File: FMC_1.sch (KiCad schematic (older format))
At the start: 16 parts, among them P1 SAMTEC_ASP-134603-01

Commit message: Convert all footprints to use Marble nickname
Includes both .sch and .lib files
Includes both bare footprint names and those with CERN-like nicknames
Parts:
- C61: footprint CAPC1005X55N -> Marble:CAPC1005X55N
- C62: footprint CAPC3216X140N -> Marble:CAPC3216X140N
- C63, C64, C65, C66, C67: footprint CAPC0603X33N -> Marble:CAPC0603X33N
- C68, C69: footprint CAPC1608X87N -> Marble:CAPC1608X87N
- F2: footprint FUSC1608X55N -> Marble:FUSC1608X55N
- P1: footprint SAMTEC_ASP-134603-01 -> Marble:SAMTEC_ASP-134603-01
- R234, R260, R261: footprint RESC1005X40N -> Marble:RESC1005X40N
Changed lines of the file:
@@
 F 0 "R234" V 10454 1260 50  0000 L CNN
 F 1 "R0402_10K_1%_0.0625W_100PPM" H 10350 990 60  0001 L CNN
-F 2 "RESC1005X40N" H 10350 180 60  0001 L CNN
+F 2 "Marble:RESC1005X40N" H 10350 180 60  0001 L CNN
 F 3 "\\\\cern.ch\\dfs\\Applications\\Altium\\Datasheets\\R0402_Phycomp_RC0402.pdf" H 10350 810 60  0001 L CNN
 F 4 "10k" V 10545 1260 50  0000 L CNN "~"
@@
 F 0 "C68" V 7796 5690 50  0000 R CNN
 F 1 "CC0603_10UF_6.3V_20%_X5R" H 7600 5540 60  0001 L CNN
-F 2 "CAPC1608X87N" H 7600 4730 60  0001 L CNN
+F 2 "Marble:CAPC1608X87N" H 7600 4730 60  0001 L CNN
 F 3 "\\\\cern.ch\\dfs\\Applications\\Altium\\Datasheets\\CC0603_X5R_KEMET.pdf" H 7600 5360 60  0001 L CNN
 F 4 "10uF" V 7705 5690 50  0000 R CNN "~"
@@
 F 0 "C67" V 7204 5610 50  0000 L CNN
 F 1 "CC0201_100NF_6.3V_10%_X5R" H 7100 5240 60  0001 L CNN
-F 2 "CAPC0603X33N" H 7100 4430 60  0001 L CNN
+F 2 "Marble:CAPC0603X33N" H 7100 4430 60  0001 L CNN
 F 3 "\\\\cern.ch\\dfs\\Applications\\Altium\\Datasheets\\CC0201_X5R_AVX.pdf" H 7100 5060 60  0001 L CNN
 F 4 "100nF" V 7295 5610 50  0000 L CNN "~"
@@
 F 0 "C69" V 8196 5690 50  0000 R CNN
 F 1 "CC0603_10UF_6.3V_20%_X5R" H 8000 5540 60  0001 L CNN
-F 2 "CAPC1608X87N" H 8000 4730 60  0001 L CNN
+F 2 "Marble:CAPC1608X87N" H 8000 4730 60  0001 L CNN
 F 3 "\\\\cern.ch\\dfs\\Applications\\Altium\\Datasheets\\CC0603_X5R_KEMET.pdf" H 8000 5360 60  0001 L CNN
 F 4 "10uF" V 8105 5690 50  0000 R CNN "~"
@@
 F 0 "C65" V 5754 6710 50  0000 L CNN
 F 1 "CC0201_100NF_6.3V_10%_X5R" H 5650 6340 60  0001 L CNN
-F 2 "CAPC0603X33N" H 5650 5530 60  0001 L CNN
+F 2 "Marble:CAPC0603X33N" H 5650 5530 60  0001 L CNN
 F 3 "\\\\cern.ch\\dfs\\Applications\\Altium\\Datasheets\\CC0201_X5R_AVX.pdf" H 5650 6160 60  0001 L CNN
 F 4 "100nF" V 5845 6710 50  0000 L CNN "~"
@@
 F 0 "C66" V 6204 6710 50  0000 L CNN
 F 1 "CC0201_100NF_6.3V_10%_X5R" H 6100 6340 60  0001 L CNN
-F 2 "CAPC0603X33N" H 6100 5530 60  0001 L CNN
+F 2 "Marble:CAPC0603X33N" H 6100 5530 60  0001 L CNN
 F 3 "\\\\cern.ch\\dfs\\Applications\\Altium\\Datasheets\\CC0201_X5R_AVX.pdf" H 6100 6160 60  0001 L CNN
 F 4 "100nF" V 6295 6710 50  0000 L CNN "~"
@@
 F 0 "C63" V 4504 5810 50  0000 L CNN
 F 1 "CC0201_100NF_6.3V_10%_X5R" H 4400 5440 60  0001 L CNN
-F 2 "CAPC0603X33N" H 4400 4630 60  0001 L CNN
+F 2 "Marble:CAPC0603X33N" H 4400 4630 60  0001 L CNN
 F 3 "\\\\cern.ch\\dfs\\Applications\\Altium\\Datasheets\\CC0201_X5R_AVX.pdf" H 4400 5260 60  0001 L CNN
 F 4 "100nF" V 4595 5810 50  0000 L CNN "~"
@@
 F 0 "C64" V 4954 5810 50  0000 L CNN
 F 1 "CC0201_100NF_6.3V_10%_X5R" H 4850 5440 60  0001 L CNN
-F 2 "CAPC0603X33N" H 4850 4630 60  0001 L CNN
+F 2 "Marble:CAPC0603X33N" H 4850 4630 60  0001 L CNN
 F 3 "\\\\cern.ch\\dfs\\Applications\\Altium\\Datasheets\\CC0201_X5R_AVX.pdf" H 4850 5260 60  0001 L CNN
 F 4 "100nF" V 5045 5810 50  0000 L CNN "~"
@@
 F 0 "C62" V 2804 5160 50  0000 L CNN
 F 1 "CC1206_10UF_16V_10%_X7R" H 2700 4790 60  0001 L CNN
-F 2 "CAPC3216X140N" H 2700 3980 60  0001 L CNN
+F 2 "Marble:CAPC3216X140N" H 2700 3980 60  0001 L CNN
 F 3 "\\\\cern.ch\\dfs\\Applications\\Altium\\Datasheets\\CC1206_X7R_KEMET.pdf" H 2700 4610 60  0001 L CNN
 F 4 "10uF" V 2895 5160 50  0000 L CNN "~"
@@
 F 0 "C61" V 2250 5050 50  0000 L CNN
 F 1 "CC0402_100NF_16V_10%_X5R" H 2200 4790 60  0001 L CNN
-F 2 "CAPC1005X55N" H 2200 3980 60  0001 L CNN
+F 2 "Marble:CAPC1005X55N" H 2200 3980 60  0001 L CNN
 F 3 "\\\\cern.ch\\dfs\\Applications\\Altium\\Datasheets\\CC0402_X5R_MURATA_GRM.pdf" H 2200 4610 60  0001 L CNN
 F 4 "100nF" V 2450 5050 50  0000 L CNN "~"
@@
 F 0 "F2" H 6700 6797 50  0000 C CNN
 F 1 "FUS0603_BOURNS-SF-0603F050-2" H 6550 6380 60  0001 L CNN
-F 2 "FUSC1608X55N" H 6550 5570 60  0001 L CNN
+F 2 "Marble:FUSC1608X55N" H 6550 5570 60  0001 L CNN
 F 3 "\\\\cern.ch\\dfs\\Applications\\Altium\\Datasheets\\FUSE_BOURNS_SF-0603F.pdf" H 6550 6200 60  0001 L CNN
 F 4 "500mA-50V" H 6700 6706 50  0000 C CNN "~"
@@
 F 0 "P1" H 4077 -500 50  0000 L CNN
 F 1 "SAMTEC_ASP-134603-01" H 3750 -2640 60  0001 L CNN
-F 2 "SAMTEC_ASP-134603-01" H 3750 -3540 60  0001 L CNN
+F 2 "Marble:SAMTEC_ASP-134603-01" H 3750 -3540 60  0001 L CNN
 F 3 "\\\\cern.ch\\dfs\\Applications\\Altium\\Datasheets\\SAMTEC_ASP-134603-01.pdf" H 3750 -2820 60  0001 L CNN
 F 4 "VITA 57" H 3750 -2910 60  0001 L CNN "Pole4"
@@
 F 0 "P1" H 6378 -500 50  0000 L CNN
 F 1 "SAMTEC_ASP-134603-01" H 6050 -2640 60  0001 L CNN
-F 2 "SAMTEC_ASP-134603-01" H 6050 -3540 60  0001 L CNN
+F 2 "Marble:SAMTEC_ASP-134603-01" H 6050 -3540 60  0001 L CNN
 F 3 "\\\\cern.ch\\dfs\\Applications\\Altium\\Datasheets\\SAMTEC_ASP-134603-01.pdf" H 6050 -2820 60  0001 L CNN
 F 4 "VITA 57" H 6050 -2910 60  0001 L CNN "Pole4"
@@
 F 0 "P1" H 9128 -500 50  0000 L CNN
 F 1 "SAMTEC_ASP-134603-01" H 8800 -2640 60  0001 L CNN
-F 2 "SAMTEC_ASP-134603-01" H 8800 -3540 60  0001 L CNN
+F 2 "Marble:SAMTEC_ASP-134603-01" H 8800 -3540 60  0001 L CNN
 F 3 "\\\\cern.ch\\dfs\\Applications\\Altium\\Datasheets\\SAMTEC_ASP-134603-01.pdf" H 8800 -2820 60  0001 L CNN
 F 4 "VITA 57" H 8800 -2910 60  0001 L CNN "Pole4"
@@
 F 0 "P1" H 11778 -500 50  0000 L CNN
 F 1 "SAMTEC_ASP-134603-01" H 11450 -2640 60  0001 L CNN
-F 2 "SAMTEC_ASP-134603-01" H 11450 -3540 60  0001 L CNN
+F 2 "Marble:SAMTEC_ASP-134603-01" H 11450 -3540 60  0001 L CNN
 F 3 "\\\\cern.ch\\dfs\\Applications\\Altium\\Datasheets\\SAMTEC_ASP-134603-01.pdf" H 11450 -2820 60  0001 L CNN
 F 4 "VITA 57" H 11450 -2910 60  0001 L CNN "Pole4"
@@
 F 0 "R260" V 5154 6660 50  0000 L CNN
 F 1 "R0402_10K_1%_0.0625W_100PPM" H 5050 6390 60  0001 L CNN
-F 2 "RESC1005X40N" H 5050 5580 60  0001 L CNN
+F 2 "Marble:RESC1005X40N" H 5050 5580 60  0001 L CNN
 F 3 "\\\\cern.ch\\dfs\\Applications\\Altium\\Datasheets\\R0402_Phycomp_RC0402.pdf" H 5050 6210 60  0001 L CNN
 F 4 "10k" V 5245 6660 50  0000 L CNN "~"
@@
 F 0 "R261" H 5550 6500 50  0000 L CNN
 F 1 "R0402_1K_1%_0.0625W_100PPM" H 5500 6390 60  0001 L CNN
-F 2 "RESC1005X40N" H 5500 5580 60  0001 L CNN
+F 2 "Marble:RESC1005X40N" H 5500 5580 60  0001 L CNN
 F 3 "\\\\cern.ch\\dfs\\Applications\\Altium\\Datasheets\\R0402_Phycomp_RC0402.pdf" H 5500 6210 60  0001 L CNN
 F 4 "1k" H 5600 6700 50  0000 L CNN "~"

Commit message: Get rid of most .DbLib suffixes in Library Name attributes
Enough that KiBoM no longer complains about them
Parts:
- R297, R298: Library Name Resistors.DbLib -> Resistors SMD
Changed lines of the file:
@@
 F 37 "10/17/12 00:00:00" H 2800 2130 50  0001 L CNN "LatestRevisionDate"
 F 38 "Resistors SMD" H 2800 2055 50  0001 L CNN "Database Table Name"
-F 39 "Resistors.DbLib" H 2800 1980 50  0001 L CNN "Library Name"
+F 39 "Resistors SMD" H 2800 1980 50  0001 L CNN "Library Name"
 F 40 "Resistors SMD" H 2800 1905 50  0001 L CNN "Footprint Library"
 F 41 "This work is licensed under the Creative Commons CC-BY-SA 4.0 License. To the extent that circuit schematics that use Licensed Material can be considered to be ‘Adapted Material’, then the copyright holder waives article 3.b of the license with respect to these schematics." H 2800 1830 50  0001 L CNN "License"
@@
 F 37 "10/17/12 00:00:00" H 4850 2230 50  0001 L CNN "LatestRevisionDate"
 F 38 "Resistors SMD" H 4850 2155 50  0001 L CNN "Database Table Name"
-F 39 "Resistors.DbLib" H 4850 2080 50  0001 L CNN "Library Name"
+F 39 "Resistors SMD" H 4850 2080 50  0001 L CNN "Library Name"
 F 40 "Resistors SMD" H 4850 2005 50  0001 L CNN "Footprint Library"
 F 41 "This work is licensed under the Creative Commons CC-BY-SA 4.0 License. To the extent that circuit schematics that use Licensed Material can be considered to be ‘Adapted Material’, then the copyright holder waives article 3.b of the license with respect to these schematics." H 4850 1930 50  0001 L CNN "License"

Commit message: Get rid of more useless inconsistencies in Comment attributes
Makes for quieter KiBoM runs
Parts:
- R297, R298: Comment 240 -> =Value
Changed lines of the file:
@@
 F 6 "Resistor - 1%" H 2800 4455 50  0001 L CNN "Library Ref"
 F 7 "SchLib\\Resistors.SchLib" H 2800 4380 50  0001 L CNN "Library Path"
-F 8 "240" H 2800 4305 50  0001 L CNN "Comment"
+F 8 "=Value" H 2800 4305 50  0001 L CNN "Comment"
 F 9 "Standard" H 2800 4230 50  0001 L CNN "Component Kind"
 F 10 "Standard" H 2800 4155 50  0001 L CNN "Component Type"
@@
 F 6 "Resistor - 1%" H 4850 4555 50  0001 L CNN "Library Ref"
 F 7 "SchLib\\Resistors.SchLib" H 4850 4480 50  0001 L CNN "Library Path"
-F 8 "240" H 4850 4405 50  0001 L CNN "Comment"
+F 8 "=Value" H 4850 4405 50  0001 L CNN "Comment"
 F 9 "Standard" H 4850 4330 50  0001 L CNN "Component Kind"
 F 10 "Standard" H 4850 4255 50  0001 L CNN "Component Type"

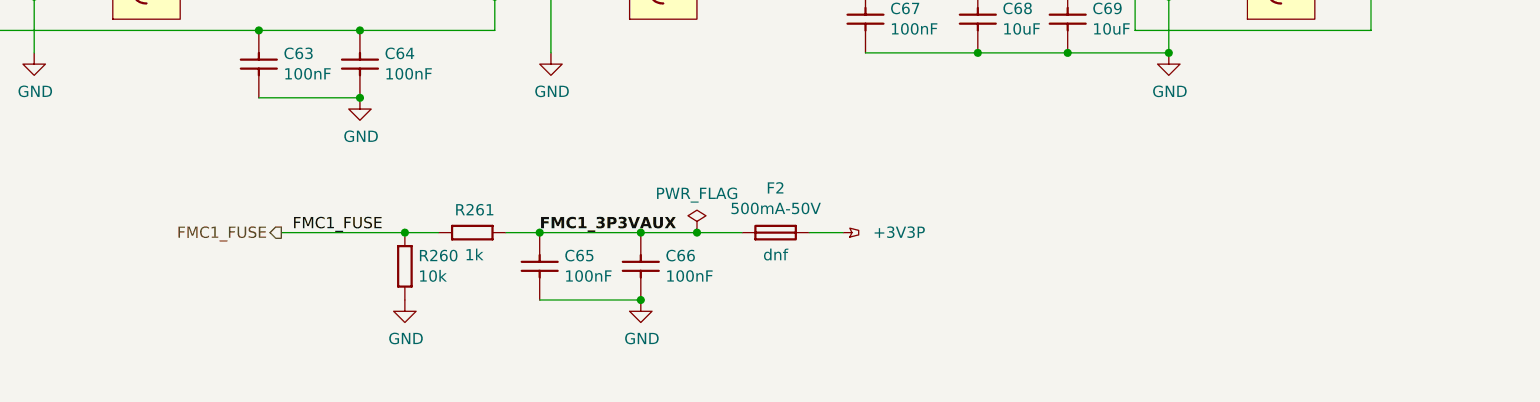
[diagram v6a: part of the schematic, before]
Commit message: added MIC2090-1
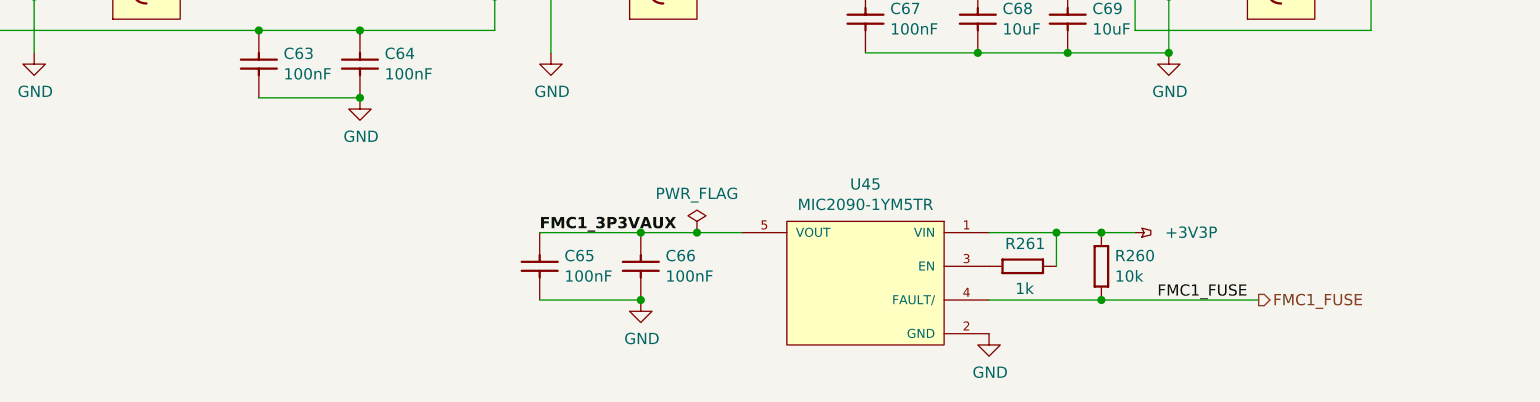
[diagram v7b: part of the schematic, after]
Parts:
- removed F2: FUS0603_BOURNS-SF-0603F050-2, Marble:FUSC1608X55N, symbol Fuses:FUS0603_BOURNS-SF-0603F050-2
- added U45: MIC2090-1YM5TR, ICs And Semiconductors SMD:SOT95P280X145-5N, symbol Analog_&_Interface:MIC2090-1YM5TR
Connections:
- net +3V3P: now also R260.1, R261.1, U45.1 (VIN)
- net FMC1_3P3VAUX: now also U45.5 (VOUT); no longer R261.1
- net FMC1_FUSE: now also R260.2, U45.4 (FAULT/); no longer R260.1, R261.2
- net GND: now also U45.2 (GND); no longer R260.2
- new net: R261.2, U45.3 (EN)
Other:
- moved on the sheet: R260, R261

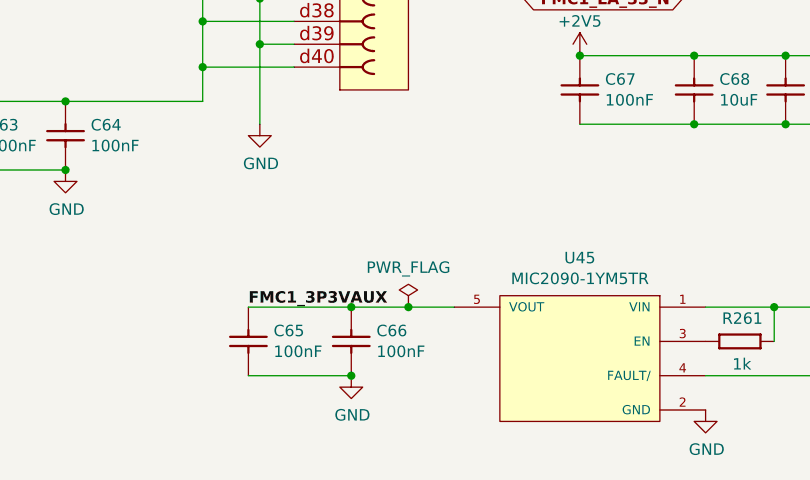
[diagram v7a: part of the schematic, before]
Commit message: remove power flag at U44, U45 VOUT-pin
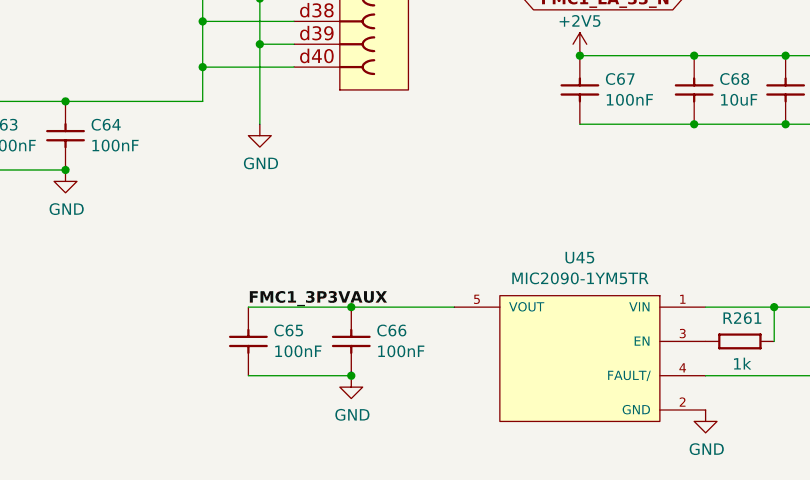
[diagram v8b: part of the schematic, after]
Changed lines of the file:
@@
 	5650 6600 6100 6600
 Connection ~ 6100 6600
-Wire Wire Line
-	6100 6600 6350 6600
 Connection ~ 6100 6900
 Wire Wire Line
@@
 	2200 5050 2700 5050
 $Comp
-L power:PWR_FLAG #FLG0119
-U 1 1 5ECD54E0
-P 6350 6600
-F 0 "#FLG0119" H 6350 6675 50  0001 C CNN
-F 1 "PWR_FLAG" H 6350 6773 50  0000 C CNN
-F 2 "" H 6350 6600 50  0001 C CNN
-F 3 "" H 6350 6600 50  0001 C CNN
-	1    6350 6600
-	1    0    0    -1
-$EndComp
-Connection ~ 6350 6600
-Wire Wire Line
-	6350 6600 6550 6600
-$Comp
 L Resistors_SMD:R0402_240R_1%_0.0625W_100PPM R297
 U 1 1 5EBC4ACC
@@
 	7650 6900 8150 6900
 Connection ~ 8150 6900
+Wire Wire Line
+	6100 6600 6550 6600
 $EndSCHEMATC
